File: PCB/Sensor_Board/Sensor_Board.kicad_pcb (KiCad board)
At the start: 2 copper layers, 90 x 90 mm, 6 parts, among them J1 Conn_01x08_Socket, J2 Conn_01x06_Socket, J3 Conn_01x04_Socket, J4 Conn_01x07_Socket, J5 Conn_01x09_Socket, J6 SE2-30

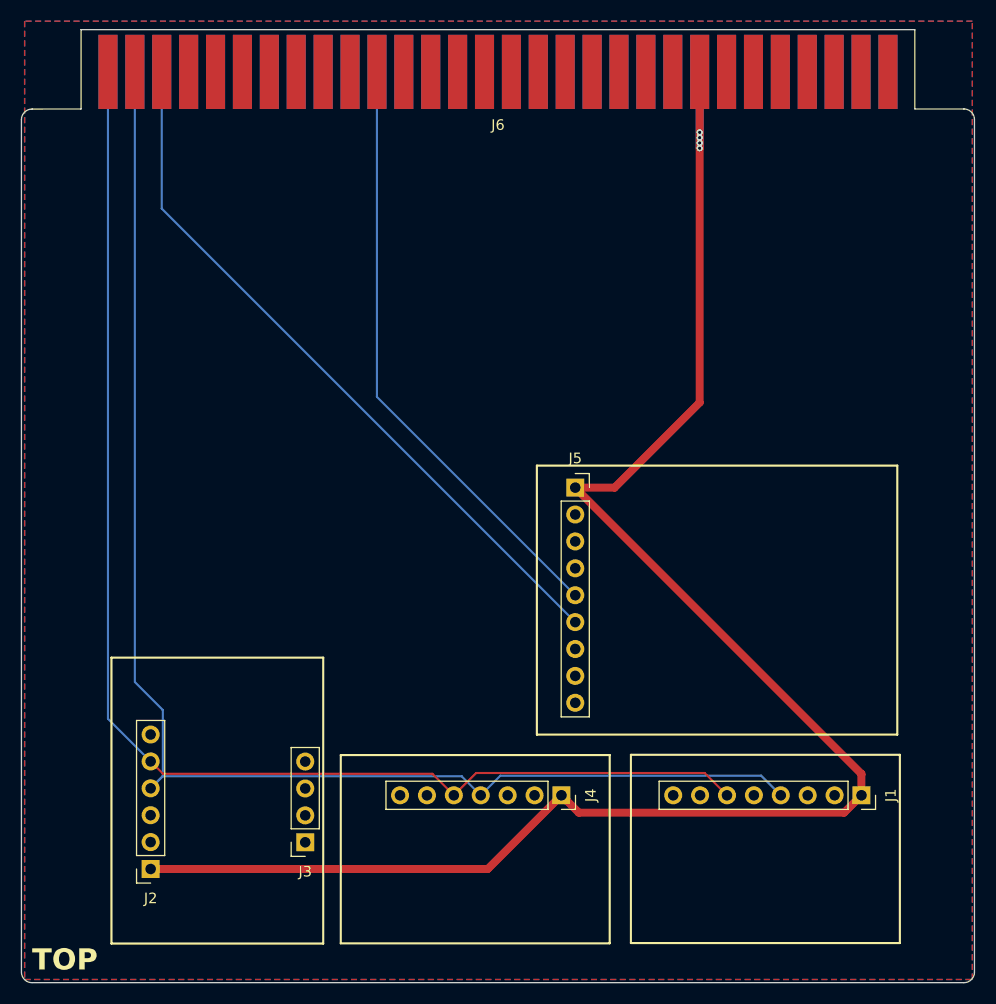
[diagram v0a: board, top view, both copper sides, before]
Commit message: updated board footprint and rerouted
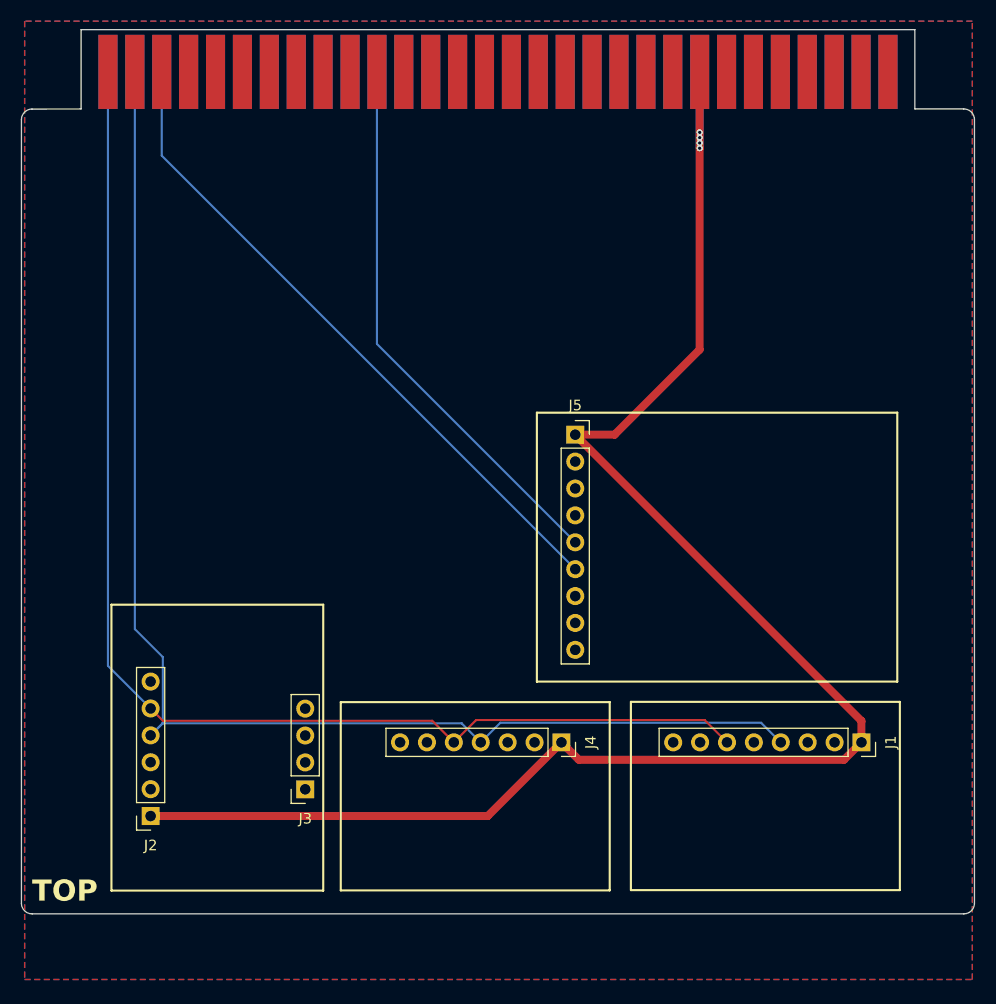
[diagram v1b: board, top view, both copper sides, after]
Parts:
- moved J2 5.00 mm to (112.4, 134.1)
- moved J3 5.00 mm to (127.0, 131.5)
- moved J5 5.00 mm to (152.5, 98.0)
- moved J1 5.00 mm to (179.5, 127.1)
- moved J4 5.00 mm to (151.2, 127.1)
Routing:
- net +3.3V: track 165.1 -> 160.1 mm
- net /TX: track 57.2 -> 52.2 mm
- net /RX: track 68.1 -> 63.1 mm
- net /SCL: track 131.5 -> 126.5 mm
- net /SDA: track 124.3 -> 119.3 mm
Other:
- board size 90 x 90 mm -> 90 x 83.5 mm
